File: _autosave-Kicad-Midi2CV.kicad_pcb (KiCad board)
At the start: 2 copper layers, 99.7 x 99.7 mm, 84 parts, among them IC1 MCP4725module, IC2 MCP4725module, J1 Doepfer connector, J10 CV4, J11 Gate1, J12 GateConn, J13 Gate2, J14 Gate3, J15 Gate4, J16 I2C_Conn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

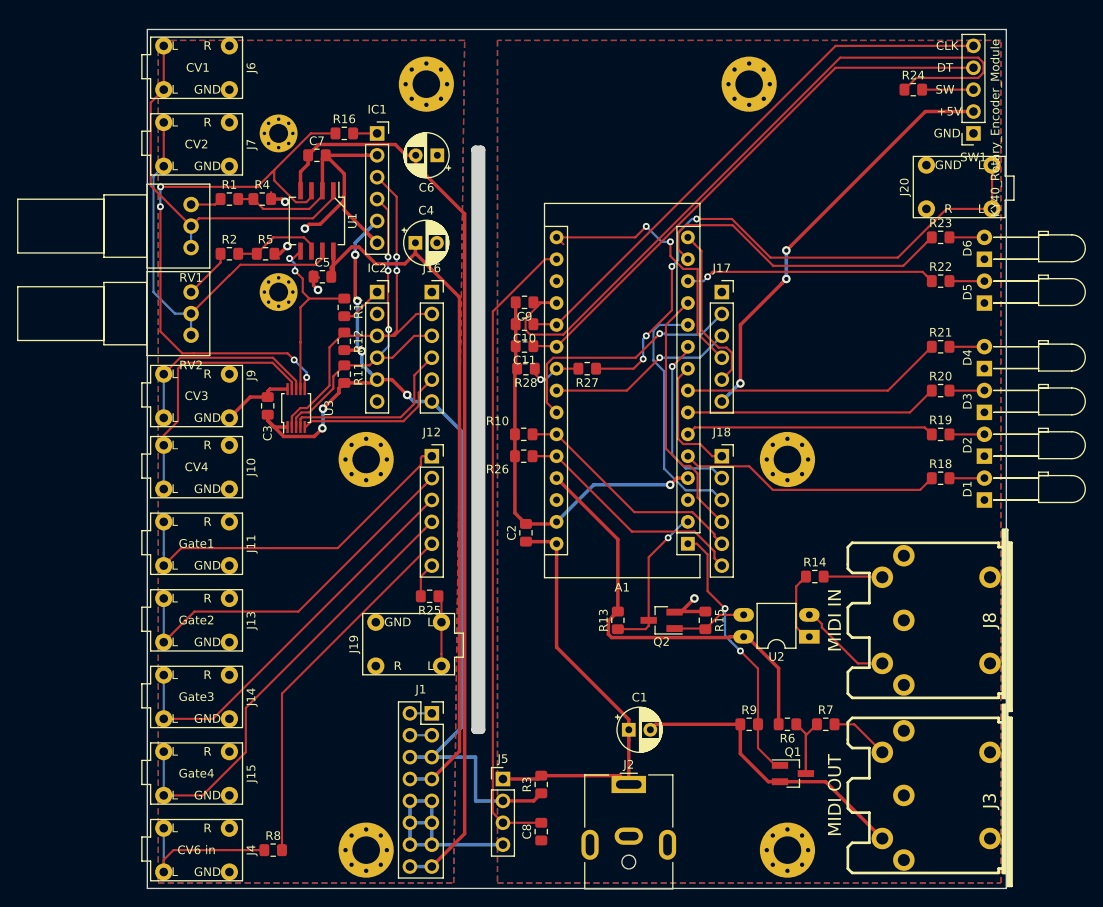
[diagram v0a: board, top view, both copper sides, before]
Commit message: PCB Final Trim
Silk adj:
Text adjustments
Label board x2
Label headers
Add values to resistors on silk

Power lanes beefed up (0,5 or 0,6) when long or feed.
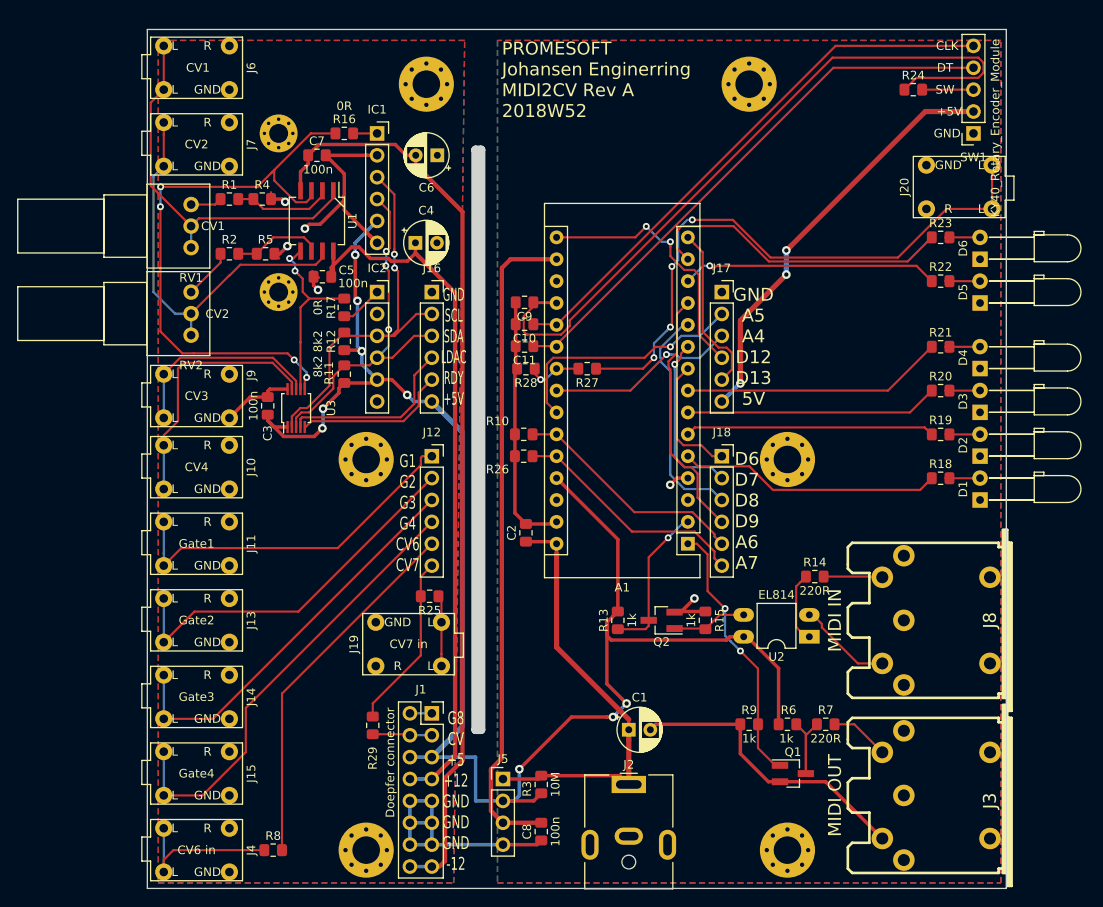
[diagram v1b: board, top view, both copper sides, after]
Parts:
- added R29: 1k, Resistor_SMD:R_0805_2012Metric_Pad1.15x1.40mm_HandSolder, F.Cu at (51.6, 106.2)
- moved D1 0.51 mm to (122.0, 80.0)
- moved D2 0.51 mm to (122.0, 74.9)
- moved D3 0.51 mm to (122.0, 69.8)
- moved D4 0.51 mm to (122.0, 64.8)
- moved D5 0.51 mm to (122.0, 57.1)
- moved D6 0.51 mm to (122.0, 52.1)
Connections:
- net Net-(J1-Pad1) renamed /Gate
- net Net-(J1-Pad3) renamed /CV
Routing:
- net +5V: track 214.5 -> 246.3 mm, vias 9 -> 12
- net A7: track 31.8 -> 48.0 mm
- net GND: track 161.4 -> 147.6 mm
- net /CV: track 2.54 -> 7.10 mm
- net Net-(A1-Pad17): track 74.2 -> 76.7 mm
- net Gate3: track 75.7 -> 73.4 mm
- net /LDAC: track 53.6 -> 52.2 mm
- net Btn: track 86.5 -> 87.5 mm
- net LED-sel: track 29.2 -> 30.1 mm
- net Net-(J20-PadT): track 68.7 -> 69.4 mm
- net /SDA: track 62.9 -> 63.6 mm
- net /12v: track 84.4 -> 83.8 mm
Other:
- board text added: "+Vin +5v +3v3 GND"
- board text added: "D6 D7 D8 D9 A6 A7"
- board text added: "G1 G2 G3 G4 CV6 CV7"
- board text added: "G8 CV +5 +12 GND GND GND -12"
- board text added: "GND A5 A4 D12 D13 5V"
- board text added: "GND SCL SDA LDAC RDY +5V"
- board text added: "PROMESOFT Johansen Enginerring MIDI2CV Rev A 2018W52"
- board text added: "PROMESOFT Johansen Enginerring SubSection - 2018W52 DAC Gate CV RevA"
- board text added: "Tip + Shield GND"
